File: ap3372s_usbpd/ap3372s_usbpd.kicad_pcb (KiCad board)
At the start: 2 copper layers, 45 x 24 mm, 26 parts, among them J10 Conn_01x03, J11 Conn_01x02, J8 USB_C_Receptacle_USB2.0_16P, J9 Conn_01x03, Q1 NMOS, Q2 NMOS, U2 AP3372S

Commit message: tidied up ap3372 board
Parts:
- moved J11 0.16 mm to (93.5, 67.1)
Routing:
- net GND2: track 160.1 -> 184.3 mm
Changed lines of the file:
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@@
 	(footprint "Connector_PinHeader_2.54mm:PinHeader_1x05_P2.54mm_Vertical"
 		(layer "F.Cu")
-		(at 93.5 66.92 180)
+		(at 93.5 67.08 180)
 		(descr "Through hole straight pin header, 1x05, 2.54mm pitch, single row")
 		(tags "Through hole pin header THT 1x05 2.54mm single row")
@@
 		(tags "SOT TO_SOT_SMD")
 		(property "Reference" "Q2"
-			(at -1.14 2.48 0)
+			(at -1.14 2.66 0)
 			(unlocked yes)
 			(layer "F.SilkS")
@@
 		(tags "capacitor handsolder")
 		(property "Reference" "C9"
-			(at -3.0325 0 0)
+			(at -3.0725 0 0)
 			(unlocked yes)
 			(layer "F.SilkS")
@@
 		(tags "capacitor handsolder")
 		(property "Reference" "C14"
-			(at -2.5575 -0.31 0)
+			(at -2.5675 -0.31 0)
 			(unlocked yes)
 			(layer "F.SilkS")
@@
 		(tags "capacitor handsolder")
 		(property "Reference" "C13"
-			(at -2.7925 0.01 0)
+			(at -3.0925 0.01 0)
 			(unlocked yes)
 			(layer "F.SilkS")
@@
 		(tags "capacitor handsolder")
 		(property "Reference" "C8"
-			(at -2.4725 -0.02 0)
+			(at -3.0725 -0.02 0)
 			(unlocked yes)
 			(layer "F.SilkS")
@@
 		(tags "resistor handsolder")
 		(property "Reference" "R14"
-			(at -4.3 0.95 180)
+			(at -4.3 -0.45 0)
 			(unlocked yes)
 			(layer "F.SilkS")
@@
 		)
 		(property "Value" "1k"
-			(at -3.94 -0.45 180)
+			(at -4.66 0.95 0)
 			(unlocked yes)
 			(layer "F.SilkS")
@@
 		(tags "resistor handsolder")
 		(property "Reference" "R11"
-			(at -1.99 -2.58 0)
+			(at -1.99 -2.66 0)
 			(unlocked yes)
 			(layer "F.SilkS")
@@
 		)
 		(property "Value" "5m"
-			(at 2.2 -2.53 0)
+			(at 2.2 -2.66 0)
 			(unlocked yes)
 			(layer "F.SilkS")
@@
 		(tags "SOT TO_SOT_SMD")
 		(property "Reference" "Q1"
-			(at -1.24 -2.41 0)
+			(at -1.24 -2.66 0)
 			(unlocked yes)
 			(layer "F.SilkS")
@@
 		)
 		(property "Value" "NMOS"
-			(at 2.47 -2.38 0)
+			(at 2.47 -2.66 0)
 			(unlocked yes)
 			(layer "F.SilkS")
@@
 		(tags "QFN NoLead")
 		(property "Reference" "U2"
-			(at 0 -3.3 0)
+			(at 0 -3.1 0)
 			(unlocked yes)
 			(layer "F.SilkS")
@@
 	)
 	(segment
-		(start 90 56.57)
-		(end 89.99 56.58)
-		(width 0.75)
-		(layer "F.Cu")
-		(net 1)
-	)
-	(segment
 		(start 52.975 72.075)
 		(end 51.9 71)
@@
 	)
 	(segment
+		(start 90.78 56.58)
+		(end 90 55.8)
+		(width 0.75)
+		(layer "F.Cu")
+		(net 1)
+	)
+	(segment
 		(start 72.25 61.75)
 		(end 72.5 62)
@@
 	)
 	(segment
-		(start 87 55.495)
-		(end 86.025 55.495)
-		(width 0.75)
-		(layer "F.Cu")
-		(net 1)
-	)
-	(segment
 		(start 81.27 63.66)
 		(end 81.28 63.67)
@@
 	)
 	(segment
-		(start 90 54.445)
-		(end 90 56.57)
-		(width 0.75)
-		(layer "F.Cu")
-		(net 1)
-	)
-	(segment
 		(start 58.2065 65.25)
 		(end 59.95 65.25)
@@
 	)
 	(segment
+		(start 87 57.6)
+		(end 87 55.495)
+		(width 0.75)
+		(layer "F.Cu")
+		(net 1)
+	)
+	(segment
 		(start 79.5 60.85)
 		(end 81.28 60.85)
@@
 	)
 	(segment
-		(start 86.025 55.495)
-		(end 85.17 56.35)
+		(start 90 55.8)
+		(end 90 54.445)
 		(width 0.75)
 		(layer "F.Cu")
@@
 	)
 	(via
-		(at 85.17 56.35)
+		(at 87 57.6)
 		(size 0.6)
 		(drill 0.3)
@@
 	)
 	(via
-		(at 89.99 56.58)
+		(at 90.78 56.58)
 		(size 0.6)
 		(drill 0.3)
@@
 	)
 	(segment
+		(start 88.25 56.35)
+		(end 90.55 56.35)
+		(width 0.75)
+		(layer "B.Cu")
+		(net 1)
+	)
+	(segment
 		(start 81.27 69.91)
 		(end 83.36 72)
@@
 	)
 	(segment
-		(start 90.78 56.58)
-		(end 93.5 59.3)
-		(width 0.75)
+		(start 93.5 64.54)
+		(end 81.99 64.54)
+		(width 1)
 		(layer "B.Cu")
 		(net 1)
@@
 	)
 	(segment
-		(start 83.98 57.54)
-		(end 85.17 56.35)
+		(start 81.99 64.38)
+		(end 81.27 63.66)
 		(width 0.75)
 		(layer "B.Cu")
@@
 	)
 	(segment
+		(start 87 57.6)
+		(end 88.25 56.35)
+		(width 0.75)
+		(layer "B.Cu")
+		(net 1)
+	)
+	(segment
+		(start 90.78 56.58)
+		(end 90.2 57.16)
+		(width 1)
+		(layer "B.Cu")
+		(net 1)
+	)
+	(segment
 		(start 65.81 57.54)
 		(end 70.82 57.54)
@@
 	)
 	(segment
-		(start 81.27 68.65)
-		(end 70.05 68.65)
+		(start 84.04 57.6)
+		(end 87 57.6)
 		(width 0.75)
 		(layer "B.Cu")
@@
 	)
 	(segment
-		(start 89.76 56.35)
-		(end 89.99 56.58)
+		(start 81.27 68.65)
+		(end 70.05 68.65)
 		(width 0.75)
 		(layer "B.Cu")
@@
 	)
 	(segment
-		(start 62.41 54.95)
-		(end 65 57.54)
-		(width 0.75)
+		(start 90.2 57.16)
+		(end 90.2 63.78)
+		(width 1)
 		(layer "B.Cu")
 		(net 1)
 	)
 	(segment
-		(start 85.17 56.35)
-		(end 89.76 56.35)
+		(start 62.41 54.95)
+		(end 65 57.54)
 		(width 0.75)
 		(layer "B.Cu")
@@
 	)
 	(segment
+		(start 93.5 59.46)
+		(end 90.2 59.46)
+		(width 1)
+		(layer "B.Cu")
+		(net 1)
+	)
+	(segment
+		(start 93.5 59.46)
+		(end 93.5 64.54)
+		(width 1)
+		(layer "B.Cu")
+		(net 1)
+	)
+	(segment
 		(start 67.655 62.275)
 		(end 67.655 66.355)
@@
 	)
 	(segment
+		(start 93.5 62)
+		(end 90.2 62)
+		(width 1)
+		(layer "B.Cu")
+		(net 1)
+	)
+	(segment
 		(start 58.6165 56.3265)
 		(end 58.16 55.87)
@@
 	)
 	(segment
-		(start 83.98 57.54)
-		(end 83.98 58.15)
+		(start 90.55 56.35)
+		(end 90.78 56.58)
 		(width 0.75)
 		(layer "B.Cu")
@@
 	)
 	(segment
-		(start 89.99 56.58)
-		(end 90.78 56.58)
+		(start 83.98 57.54)
+		(end 84.04 57.6)
 		(width 0.75)
 		(layer "B.Cu")
@@
 	)
 	(segment
-		(start 93.5 59.3)
-		(end 93.5 64.38)
+		(start 83.98 57.54)
+		(end 83.98 58.15)
 		(width 0.75)
 		(layer "B.Cu")
@@
 	)
 	(segment
+		(start 81.99 64.54)
+		(end 81.99 64.38)
+		(width 0.75)
+		(layer "B.Cu")
+		(net 1)
+	)
+	(segment
 		(start 67.99 61.94)
 		(end 67.655 62.275)
@@
 	)
 	(segment
+		(start 90.2 63.78)
+		(end 89.44 64.54)
+		(width 1)
+		(layer "B.Cu")
+		(net 1)
+	)
+	(segment
 		(start 81.27 68.65)
 		(end 81.27 69.91)
@@
 	)
 	(segment
-		(start 88.69 52.37)
-		(end 90 52.37)
+		(start 91.7 58.72)
+		(end 91.7 65.28)
 		(width 0.75)
 		(layer "F.Cu")
@@
 	)
 	(segment
-		(start 93.5 70.4)
-		(end 92.9 71)
+		(start 88.69 52.37)
+		(end 90 52.37)
 		(width 0.75)
 		(layer "F.Cu")
@@
 	)
 	(segment
-		(start 92.025 65.605)
-		(end 93.5 67.08)
+		(start 93.5 70.4)
+		(end 92.9 71)
 		(width 0.75)
 		(layer "F.Cu")
@@
 	)
 	(segment
-		(start 93.5 67.08)
-		(end 93.5 70.4)
+		(start 93.5 56.92)
+		(end 91.7 58.72)
 		(width 0.75)
 		(layer "F.Cu")
@@
 	)
 	(segment
-		(start 86.9925 52.3625)
-		(end 87 52.37)
+		(start 93.5 55.87)
+		(end 93.5 56.92)
 		(width 0.75)
 		(layer "F.Cu")
@@
 	)
 	(segment
-		(start 92.025 58.395)
-		(end 92.025 65.605)
+		(start 86.9925 52.3625)
+		(end 87 52.37)
 		(width 0.75)
 		(layer "F.Cu")
@@
 	)
 	(segment
-		(start 93.5 55.87)
-		(end 93.5 56.92)
+		(start 91.7 65.28)
+		(end 93.5 67.08)
 		(width 0.75)
 		(layer "F.Cu")
@@
 	)
 	(segment
-		(start 88.69 58.26)
-		(end 87.52 59.43)
-		(width 0.25)
+		(start 90 52.37)
+		(end 93.5 55.87)
+		(width 0.75)
 		(layer "F.Cu")
 		(net 13)
 	)
 	(segment
-		(start 93.5 56.92)
-		(end 92.025 58.395)
-		(width 0.75)
+		(start 88.69 58.26)
+		(end 87.52 59.43)
+		(width 0.25)
 		(layer "F.Cu")
 		(net 13)
 	)
 	(segment
-		(start 90 52.37)
-		(end 93.5 55.87)
+		(start 93.5 67.08)
+		(end 93.5 70.4)
 		(width 0.75)
 		(layer "F.Cu")
@@
 			)
 		)
+	)
+	(zone
+		(net 0)
+		(net_name "")
+		(layers "F&B.Cu")
+		(hatch edge 0.5)
+		(connect_pads
+			(clearance 0)
+		)
+		(min_thickness 0.25)
+		(filled_areas_thickness no)
+		(keepout
+			(tracks allowed)
+			(vias allowed)
+			(pads allowed)
+			(copperpour not_allowed)
+			(footprints allowed)
+		)
+		(fill
+			(thermal_gap 0.5)
+			(thermal_bridge_width 0.5)
+		)
+		(polygon
+			(pts
+				(xy 92.17 55.43) (xy 94.83 55.43) (xy 94.83 68.2) (xy 92.2 68.2)
+			)
+		)

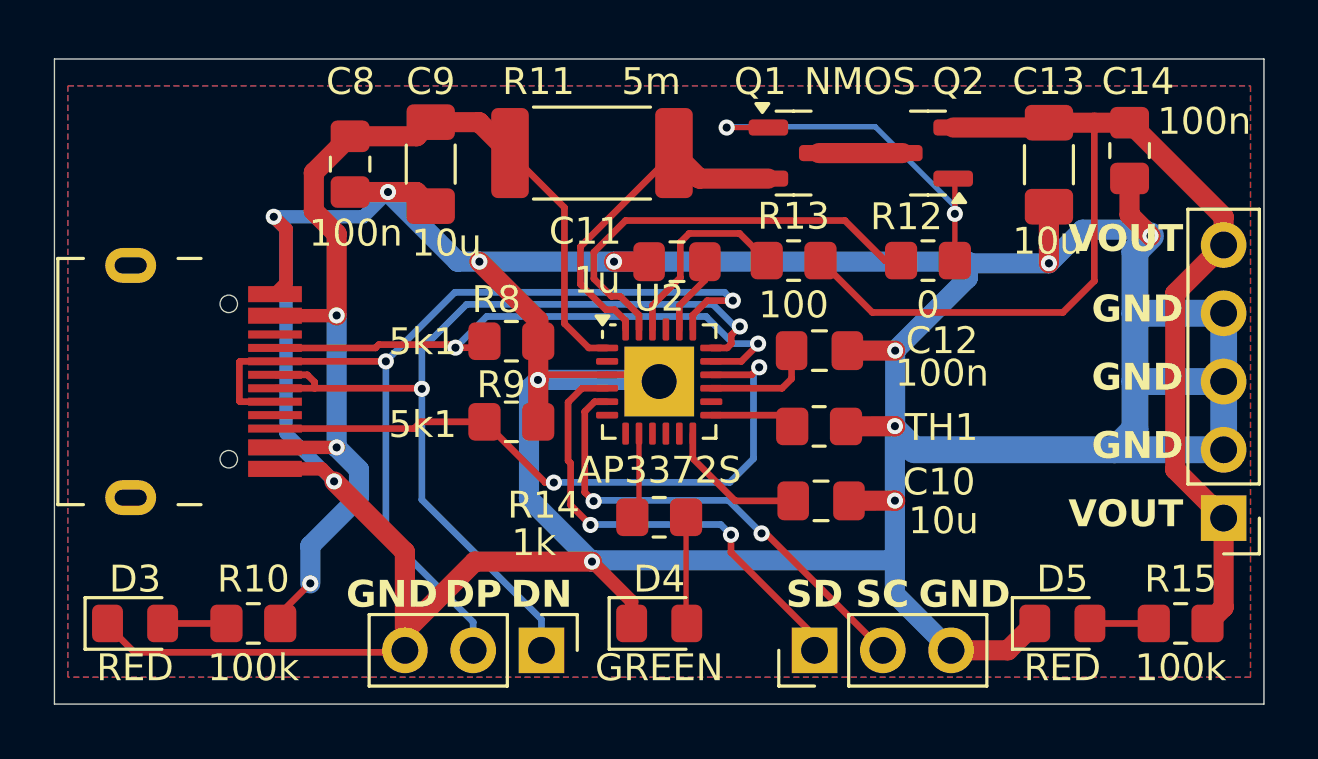
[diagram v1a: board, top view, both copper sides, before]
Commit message: added DFN breakout changed trim pot type in 33063_boost, 33063_invert, r1283_power boards fixed error in 33063_boost board (move trim pot to higher side of voltage divider)
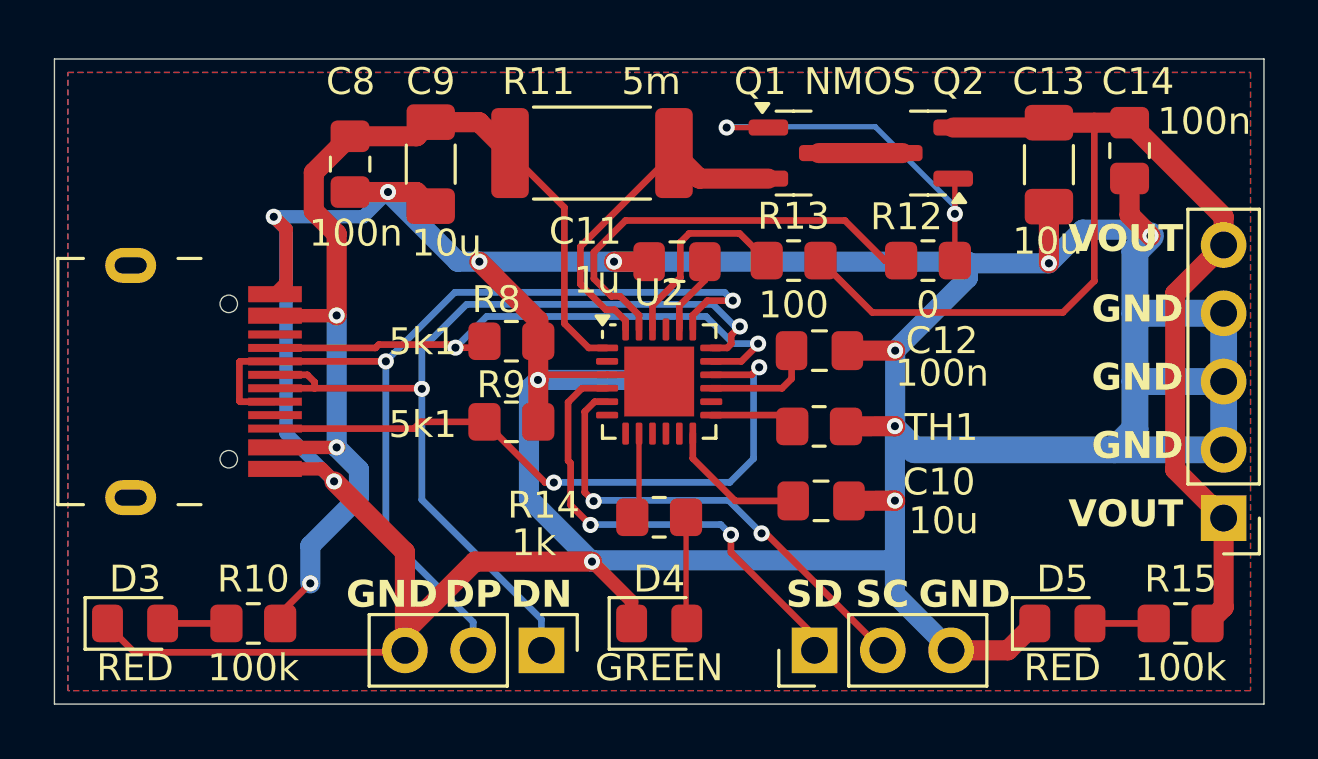
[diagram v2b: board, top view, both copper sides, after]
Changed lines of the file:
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@@
 		(tags "QFN NoLead")
 		(property "Reference" "U2"
-			(at 0 -3.1 0)
-			(unlocked yes)
+			(at 0 -3.3 0)
 			(layer "F.SilkS")
 			(effects
@@
 		(property "Value" "AP3372S"
 			(at 0 3.3 0)
-			(unlocked yes)
-			(layer "F.SilkS")
+			(layer "F.Fab")
 			(effects
 				(font
@@
 		(fp_text user "${REFERENCE}"
 			(at 0 0 0)
-			(unlocked yes)
 			(layer "F.Fab")
 			(effects
@@
 			)
 		)
+		(pad "" smd roundrect
+			(at -0.65 -0.65)
+			(size 1.05 1.05)
+			(layers "F.Paste")
+			(roundrect_rratio 0.238095)
+		)
+		(pad "" smd roundrect
+			(at -0.65 0.65)
+			(size 1.05 1.05)
+			(layers "F.Paste")
+			(roundrect_rratio 0.238095)
+		)
+		(pad "" smd roundrect
+			(at 0.65 -0.65)
+			(size 1.05 1.05)
+			(layers "F.Paste")
+			(roundrect_rratio 0.238095)
+		)
+		(pad "" smd roundrect
+			(at 0.65 0.65)
+			(size 1.05 1.05)
+			(layers "F.Paste")
+			(roundrect_rratio 0.238095)
+		)
 		(pad "1" smd roundrect
 			(at -1.9375 -1.25)
@@
 			(pintype "input")
 		)
-		(pad "25" thru_hole rect
+		(pad "25" smd rect
 			(at 0 0)
 			(size 2.6 2.6)
-			(drill 1.3)
 			(property pad_prop_heatsink)
-			(layers "*.Cu" "*.Mask")
-			(remove_unused_layers no)
+			(layers "F.Cu" "F.Mask")
 			(net 1 "GND2")
 			(pinfunction "EP")
@@
 		(polygon
 			(pts
-				(xy 50.5 51) (xy 94.5 51) (xy 94.5 73) (xy 50.5 73)
-			)
-		)
+				(xy 50.5 50.5) (xy 94.5 50.5) (xy 94.5 73.5) (xy 50.5 73.5)
+			)
+		)
